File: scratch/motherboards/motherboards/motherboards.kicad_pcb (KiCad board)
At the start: 2 copper layers, 34.6 x 90.2 mm, 8 parts, among them J101 Conn_01x35, J102 Conn_02x35_Counter_Clockwise, J103 Conn_01x35, J104 Conn_01x35, J105 Conn_02x35_Counter_Clockwise, J106 Conn_01x35

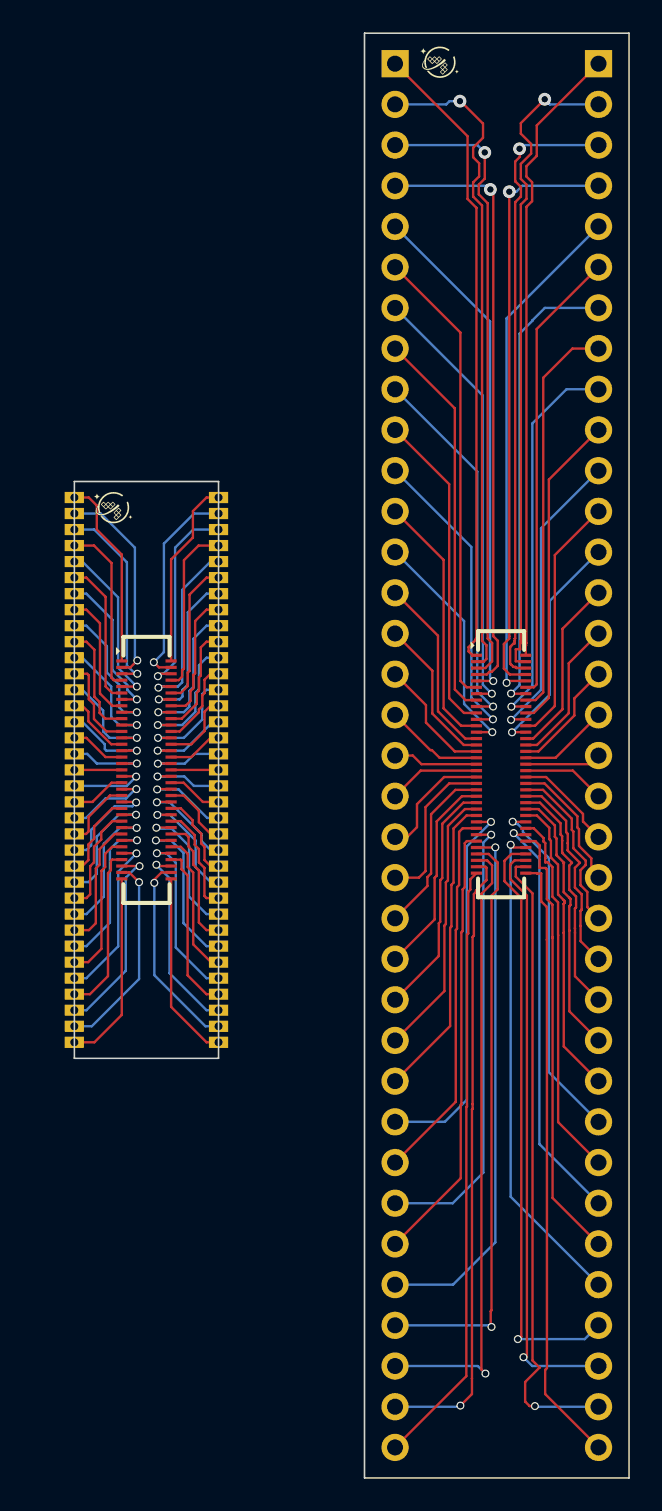
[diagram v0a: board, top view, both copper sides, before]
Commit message: create more pretty symbols for mezzanine and padring
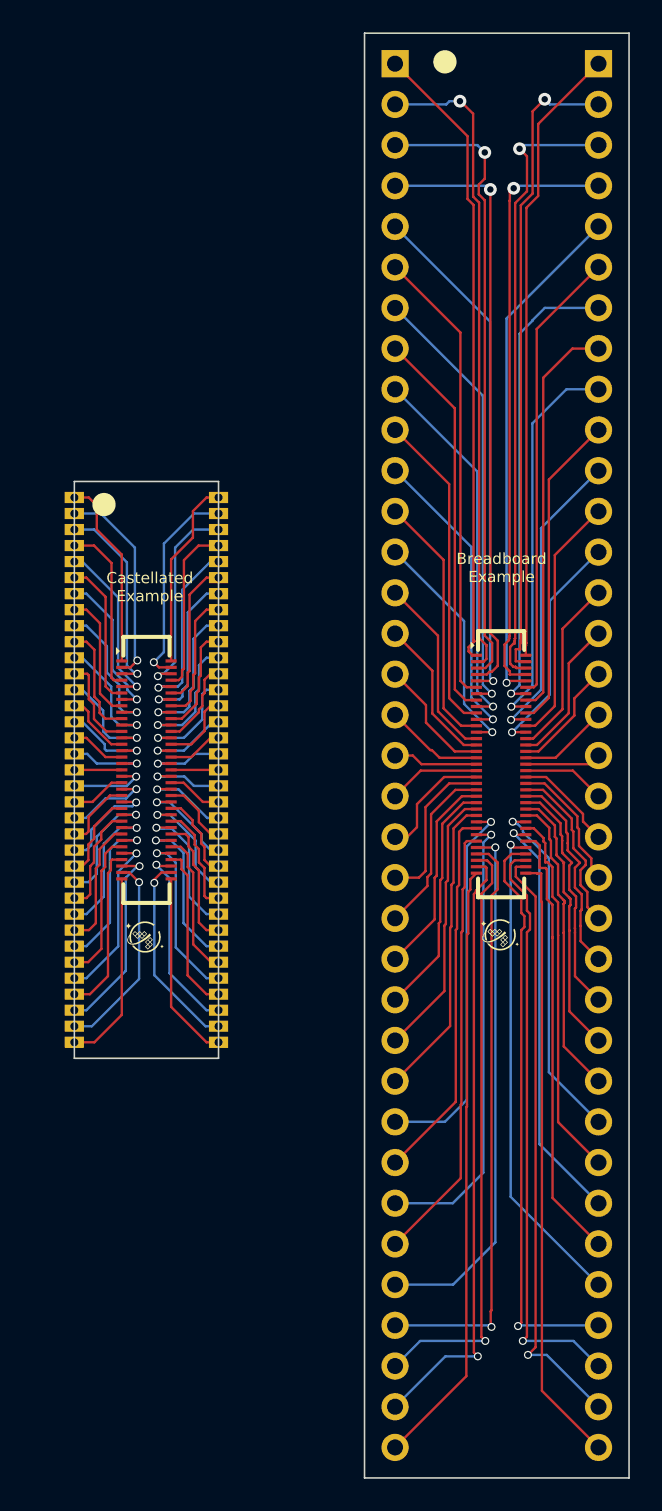
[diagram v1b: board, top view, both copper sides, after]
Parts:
- moved G*** 54.6 mm to (123.8, 78.0)
- moved G*** 26.9 mm to (101.6, 78.1)
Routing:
- net Net-(J102-Pin_37): track 39.7 -> 37.5 mm
- net Net-(J101-Pin_33): track 39.0 -> 37.5 mm
- net Net-(J102-Pin_39): track 37.3 -> 36.3 mm
- net Net-(J101-Pin_34): track 39.0 -> 38.0 mm
- net Net-(J102-Pin_69): track 40.9 -> 40.1 mm
- net Net-(J101-Pin_2): track 41.2 -> 40.4 mm
- net Net-(J102-Pin_38): track 37.4 -> 36.9 mm
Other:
- board text added: "Breadboard Example"
- board text added: "Castellated Example"

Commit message: housekeeping
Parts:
- removed J102, J105: Conn_02x35_Counter_Clockwise, Connector_Mezzanine:CONN-SMD_70P-P0.40_HC-PBB40C-70DS-0.4V-3.0-02
- added U1: ~, WaferSpace:P0.40_HC-PBB40C-70DS-0.4V-3.0-02_wscob, F.Cu at (123.8, 67.5)
- added U2: ~, WaferSpace:P0.40_HC-PBB40C-70DS-0.4V-3.0-02_wscob, F.Cu at (101.7, 67.8)
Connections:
- J101 pad 10: Net-(J101-Pin_10) -> /GND
- J101 pad 17: Net-(J101-Pin_17) -> /PWR_AUX
- J101 pad 18: Net-(J101-Pin_18) -> /GND
- J101 pad 25: Net-(J101-Pin_25) -> /VDD_CORE
- J101 pad 26: Net-(J101-Pin_26) -> /GND
- J101 pad 27: Net-(J101-Pin_27) -> /VDD_IO
- J101 pad 9: Net-(J101-Pin_9) -> /VDD_IO
- J103 pad 10: Net-(J102-Pin_61) -> /GND
- J103 pad 11: Net-(J102-Pin_60) -> /VDD_CORE
- J103 pad 18: Net-(J102-Pin_53) -> /GND
- J103 pad 19: Net-(J102-Pin_52) -> /PWR_AUX
- J103 pad 24: Net-(J102-Pin_47) -> /VDD_IO
- J103 pad 25: Net-(J102-Pin_46) -> /GND
- J103 pad 9: Net-(J102-Pin_62) -> /VDD_IO
- J104 pad 10: Net-(J104-Pin_10) -> /GND
- J104 pad 17: Net-(J104-Pin_17) -> /PWR_AUX
- J104 pad 18: Net-(J104-Pin_18) -> /GND
- J104 pad 25: Net-(J104-Pin_25) -> /VDD_CORE
- J104 pad 26: Net-(J104-Pin_26) -> /GND
- J104 pad 27: Net-(J104-Pin_27) -> /VDD_IO
- J104 pad 9: Net-(J104-Pin_9) -> /VDD_IO
- J106 pad 10: Net-(J105-Pin_61) -> /GND
- J106 pad 11: Net-(J105-Pin_60) -> /VDD_CORE
- J106 pad 18: Net-(J105-Pin_53) -> /GND
- J106 pad 19: Net-(J105-Pin_52) -> /PWR_AUX
- J106 pad 24: Net-(J105-Pin_47) -> /VDD_IO
- J106 pad 25: Net-(J105-Pin_46) -> /GND
- J106 pad 9: Net-(J105-Pin_62) -> /VDD_IO
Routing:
- net /VDD_IO: track 0.00 -> 131.0 mm, vias 0 -> 7
- net /GND: track 0.00 -> 121.6 mm, vias 0 -> 22
- net /VDD_CORE: track 0.00 -> 59.5 mm, vias 0 -> 3
- net /PWR_AUX: track 0.00 -> 28.0 mm, vias 0 -> 4
- net Net-(J102-Pin_62): track 24.1 -> 0.00 mm, vias 1 -> 0
- net Net-(J101-Pin_27): track 23.9 -> 0.00 mm, vias 1 -> 0
- net Net-(J101-Pin_9): track 23.4 -> 0.00 mm, vias 1 -> 0
- net Net-(J101-Pin_10): track 20.2 -> 0.00 mm
- net Net-(J102-Pin_61): track 19.8 -> 0.00 mm
- net Net-(J101-Pin_26): track 19.0 -> 0.00 mm
- net Net-(J102-Pin_60): track 18.7 -> 0.00 mm, vias 1 -> 0
- net Net-(J101-Pin_25): track 17.0 -> 0.00 mm
- net Net-(J102-Pin_46): track 16.9 -> 0.00 mm
- net Net-(J102-Pin_47): track 14.9 -> 0.00 mm
- net Net-(J105-Pin_62): track 9.13 -> 0.00 mm, vias 1 -> 0
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- added copper zone on B.Cu, net /GND
- added copper zone on F.Cu, net /GND

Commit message: pcb order sent with this
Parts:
- moved J104 0.66 mm to (96.5, 68.0)
- moved J106 0.42 mm to (106.5, 68.0)
- moved G*** 0.25 mm to (101.4, 78.3)
- moved U2 0.25 mm to (101.5, 68.0)
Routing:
- net /GND: vias 22 -> 26
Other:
- board size 34.6 x 90.2 mm -> 35.2 x 90.2 mm
